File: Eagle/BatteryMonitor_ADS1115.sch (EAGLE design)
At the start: 15 parts, among them IC1 MCP1703CB

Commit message: Optimize part placement
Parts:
- C2, C3, C5: value 100n -> 1µ
- C4: value 100n -> 2µ
- C7: value 100n -> 10µ
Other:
- moved on the sheet: C5
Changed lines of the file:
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@@
 <?xml version="1.0" encoding="utf-8"?>
 <!DOCTYPE eagle SYSTEM "eagle.dtd">
-<eagle version="7.2.0">
+<eagle version="9.6.2">
 <drawing>
 <settings>
 <setting alwaysvectorfont="no"/>
+<setting keepoldvectorfont="yes"/>
 <setting verticaltext="up"/>
 </settings>
@@
 <part name="R2" library="eagle-ltspice" deviceset="R" device="R1206" value="10k"/>
 <part name="C1" library="rcl" deviceset="C-EU" device="C1206" value="100n"/>
-<part name="C2" library="rcl" deviceset="C-EU" device="C1206" value="100n"/>
-<part name="C3" library="rcl" deviceset="C-EU" device="C1206" value="100n"/>
-<part name="C4" library="rcl" deviceset="C-EU" device="C1206" value="100n"/>
+<part name="C2" library="rcl" deviceset="C-EU" device="C1206" value="1µ"/>
+<part name="C3" library="rcl" deviceset="C-EU" device="C1206" value="1µ"/>
+<part name="C4" library="rcl" deviceset="C-EU" device="C1206" value="2µ"/>
 <part name="GND1" library="supply1" deviceset="GND" device=""/>
 <part name="P+1" library="supply1" deviceset="VCC" device=""/>
 <part name="D1" library="diode" deviceset="CGRM400*-G" device="" technology="1"/>
-<part name="C7" library="resistor" deviceset="C-EU" device="C4532" value="100n"/>
+<part name="C7" library="resistor" deviceset="C-EU" device="C4532" value="10µ"/>
 <part name="IC1" library="linear" deviceset="MCP1703" device="CB"/>
-<part name="C5" library="rcl" deviceset="C-EU" device="C1206" value="100n"/>
+<part name="C5" library="rcl" deviceset="C-EU" device="C1206" value="1µ"/>
 </parts>
 <sheets>
@@
 </plain>
 <instances>
-<instance part="U$1" gate="G$1" x="101.6" y="66.04"/>
-<instance part="HSTS016L" gate="A" x="152.4" y="2.54"/>
-<instance part="PWR" gate="-1" x="-7.62" y="43.18">
+<instance part="U$1" gate="G$1" x="101.6" y="66.04" smashed="yes">
+<attribute name="NAME" x="99.06" y="88.9" size="1.27" layer="95"/>
+<attribute name="VALUE" x="99.06" y="86.36" size="1.27" layer="96"/>
+</instance>
+<instance part="HSTS016L" gate="A" x="152.4" y="2.54" smashed="yes">
+<attribute name="NAME" x="146.05" y="10.795" size="1.778" layer="95"/>
+<attribute name="VALUE" x="146.05" y="-5.08" size="1.778" layer="96"/>
+</instance>
+<instance part="PWR" gate="-1" x="-7.62" y="43.18" smashed="yes">
 <attribute name="VIN" x="-7.62" y="38.1" size="1.778" layer="96"/>
-</instance>
-<instance part="PWR" gate="-2" x="-7.62" y="48.26">
+<attribute name="NAME" x="-7.62" y="44.069" size="1.778" layer="95" rot="R180"/>
+</instance>
+<instance part="PWR" gate="-2" x="-7.62" y="48.26" smashed="yes">
 <attribute name="GND" x="-7.62" y="50.8" size="1.778" layer="96" display="name"/>
-</instance>
-<instance part="U$2" gate="G$1" x="101.6" y="7.62"/>
-<instance part="U$3" gate="G$1" x="48.26" y="53.34"/>
-<instance part="R1" gate="G$1" x="17.78" y="30.48" rot="R90"/>
-<instance part="R2" gate="G$1" x="17.78" y="12.7" rot="R90"/>
-<instance part="C1" gate="G$1" x="27.94" y="12.7"/>
-<instance part="C2" gate="G$1" x="30.48" y="83.82"/>
-<instance part="C3" gate="G$1" x="50.8" y="83.82"/>
-<instance part="C4" gate="G$1" x="40.64" y="83.82"/>
-<instance part="GND1" gate="1" x="30.48" y="71.12"/>
-<instance part="P+1" gate="VCC" x="30.48" y="96.52"/>
-<instance part="D1" gate="G$1" x="7.62" y="43.18"/>
-<instance part="C7" gate="G$1" x="17.78" y="81.28" rot="R180"/>
-<instance part="IC1" gate="G$1" x="53.34" y="27.94"/>
-<instance part="C5" gate="G$1" x="7.62" y="83.82"/>
+<attribute name="VALUE" x="-10.16" y="44.577" size="1.778" layer="96"/>
+<attribute name="NAME" x="-7.62" y="49.149" size="1.778" layer="95" rot="R180"/>
+</instance>
+<instance part="U$2" gate="G$1" x="101.6" y="7.62" smashed="yes">
+<attribute name="NAME" x="91.44" y="22.86" size="1.27" layer="94"/>
+<attribute name="VALUE" x="91.44" y="20.32" size="1.27" layer="94"/>
+</instance>
+<instance part="U$3" gate="G$1" x="48.26" y="53.34" smashed="yes">
+<attribute name="NAME" x="33.02" y="55.88" size="1.27" layer="94"/>
+<attribute name="VALUE" x="33.02" y="35.56" size="1.27" layer="94"/>
+</instance>
+<instance part="R1" gate="G$1" x="17.78" y="30.48" smashed="yes" rot="R90">
+<attribute name="NAME" x="16.2814" y="26.67" size="1.778" layer="95" rot="R90"/>
+<attribute name="VALUE" x="21.082" y="26.67" size="1.778" layer="96" rot="R90"/>
+</instance>
+<instance part="R2" gate="G$1" x="17.78" y="12.7" smashed="yes" rot="R90">
+<attribute name="NAME" x="16.2814" y="8.89" size="1.778" layer="95" rot="R90"/>
+<attribute name="VALUE" x="21.082" y="8.89" size="1.778" layer="96" rot="R90"/>
+</instance>
+<instance part="C1" gate="G$1" x="27.94" y="12.7" smashed="yes">
+<attribute name="NAME" x="29.464" y="13.081" size="1.778" layer="95"/>
+<attribute name="VALUE" x="29.464" y="8.001" size="1.778" layer="96"/>
+</instance>
+<instance part="C2" gate="G$1" x="30.48" y="83.82" smashed="yes">
+<attribute name="NAME" x="32.004" y="84.201" size="1.778" layer="95"/>
+<attribute name="VALUE" x="32.004" y="79.121" size="1.778" layer="96"/>
+</instance>
+<instance part="C3" gate="G$1" x="50.8" y="83.82" smashed="yes">
+<attribute name="NAME" x="52.324" y="84.201" size="1.778" layer="95"/>
+<attribute name="VALUE" x="52.324" y="79.121" size="1.778" layer="96"/>
+</instance>
+<instance part="C4" gate="G$1" x="40.64" y="83.82" smashed="yes">
+<attribute name="NAME" x="42.164" y="84.201" size="1.778" layer="95"/>
+<attribute name="VALUE" x="42.164" y="79.121" size="1.778" layer="96"/>
+</instance>
+<instance part="GND1" gate="1" x="30.48" y="71.12" smashed="yes">
+<attribute name="VALUE" x="27.94" y="68.58" size="1.778" layer="96"/>
+</instance>
+<instance part="P+1" gate="VCC" x="30.48" y="96.52" smashed="yes">
+<attribute name="VALUE" x="27.94" y="93.98" size="1.778" layer="96" rot="R90"/>
+</instance>
+<instance part="D1" gate="G$1" x="7.62" y="43.18" smashed="yes">
+<attribute name="NAME" x="10.16" y="43.6626" size="1.778" layer="95"/>
+<attribute name="VALUE" x="10.16" y="40.8686" size="1.778" layer="96"/>
+</instance>
+<instance part="C7" gate="G$1" x="17.78" y="81.28" smashed="yes" rot="R180">
+<attribute name="NAME" x="16.256" y="80.899" size="1.778" layer="95" rot="R180"/>
+<attribute name="VALUE" x="16.256" y="85.979" size="1.778" layer="96" rot="R180"/>
+</instance>
+<instance part="IC1" gate="G$1" x="53.34" y="27.94" smashed="yes">
+<attribute name="NAME" x="45.72" y="33.655" size="1.778" layer="95"/>
+<attribute name="VALUE" x="45.72" y="31.115" size="1.778" layer="96"/>
+</instance>
+<instance part="C5" gate="G$1" x="2.54" y="83.82" smashed="yes">
+<attribute name="NAME" x="4.064" y="84.201" size="1.778" layer="95"/>
+<attribute name="VALUE" x="4.064" y="79.121" size="1.778" layer="96"/>
+</instance>
 </instances>
 <busses>
@@
 <wire x1="50.8" y1="73.66" x2="50.8" y2="78.74" width="0.1524" layer="91"/>
 <pinref part="C5" gate="G$1" pin="2"/>
-<wire x1="7.62" y1="78.74" x2="7.62" y2="73.66" width="0.1524" layer="91"/>
-<wire x1="7.62" y1="73.66" x2="17.78" y2="73.66" width="0.1524" layer="91"/>
+<wire x1="2.54" y1="78.74" x2="2.54" y2="73.66" width="0.1524" layer="91"/>
+<wire x1="2.54" y1="73.66" x2="17.78" y2="73.66" width="0.1524" layer="91"/>
 <junction x="40.64" y="73.66"/>
 <junction x="17.78" y="73.66"/>
@@
 <wire x1="17.78" y1="88.9" x2="17.78" y2="86.36" width="0.1524" layer="91"/>
 <pinref part="C5" gate="G$1" pin="1"/>
-<wire x1="7.62" y1="86.36" x2="7.62" y2="88.9" width="0.1524" layer="91"/>
-<wire x1="7.62" y1="88.9" x2="17.78" y2="88.9" width="0.1524" layer="91"/>
+<wire x1="2.54" y1="86.36" x2="2.54" y2="88.9" width="0.1524" layer="91"/>
+<wire x1="2.54" y1="88.9" x2="17.78" y2="88.9" width="0.1524" layer="91"/>
 <junction x="17.78" y="88.9"/>
 </segment>

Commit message: Change layout - all SMD on top
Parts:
- renumbered HSTS016L to I-SENS, U$1 to ESP32
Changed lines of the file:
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@@
 </classes>
 <parts>
-<part name="U$1" library="MH-ET_ESP32_D1_MINI" deviceset="MH-ET_ESP32_D1_MINI" device=""/>
-<part name="HSTS016L" library="pinhead" deviceset="PINHD-1X4" device="/90" value="1"/>
+<part name="ESP32" library="MH-ET_ESP32_D1_MINI" deviceset="MH-ET_ESP32_D1_MINI" device=""/>
+<part name="I-SENS" library="pinhead" deviceset="PINHD-1X4" device="/90" value="1"/>
 <part name="PWR" library="con-wago-500" deviceset="W237-102" device="" value="12V">
 <attribute name="GND" value=""/>
@@
 </plain>
 <instances>
-<instance part="U$1" gate="G$1" x="101.6" y="66.04" smashed="yes">
+<instance part="ESP32" gate="G$1" x="101.6" y="66.04" smashed="yes">
 <attribute name="NAME" x="99.06" y="88.9" size="1.27" layer="95"/>
 <attribute name="VALUE" x="99.06" y="86.36" size="1.27" layer="96"/>
 </instance>
-<instance part="HSTS016L" gate="A" x="152.4" y="2.54" smashed="yes">
+<instance part="I-SENS" gate="A" x="152.4" y="2.54" smashed="yes">
 <attribute name="NAME" x="146.05" y="10.795" size="1.778" layer="95"/>
 <attribute name="VALUE" x="146.05" y="-5.08" size="1.778" layer="96"/>
@@
 <net name="GND" class="0">
 <segment>
-<pinref part="U$1" gate="G$1" pin="GND@1"/>
+<pinref part="ESP32" gate="G$1" pin="GND@1"/>
 <wire x1="86.36" y1="81.28" x2="66.04" y2="81.28" width="0.1524" layer="91"/>
 <wire x1="66.04" y1="81.28" x2="66.04" y2="50.8" width="0.1524" layer="91"/>
@@
 <wire x1="66.04" y1="48.26" x2="66.04" y2="50.8" width="0.1524" layer="91"/>
 <junction x="66.04" y="50.8"/>
-<pinref part="U$1" gate="G$1" pin="GND@2"/>
+<pinref part="ESP32" gate="G$1" pin="GND@2"/>
 <wire x1="116.84" y1="66.04" x2="127" y2="66.04" width="0.1524" layer="91"/>
 <wire x1="127" y1="66.04" x2="127" y2="96.52" width="0.1524" layer="91"/>
@@
 <wire x1="66.04" y1="96.52" x2="66.04" y2="81.28" width="0.1524" layer="91"/>
 <junction x="66.04" y="81.28"/>
-<pinref part="U$1" gate="G$1" pin="GND@3"/>
+<pinref part="ESP32" gate="G$1" pin="GND@3"/>
 <wire x1="116.84" y1="55.88" x2="127" y2="55.88" width="0.1524" layer="91"/>
 <wire x1="127" y1="55.88" x2="127" y2="66.04" width="0.1524" layer="91"/>
@@
 <junction x="66.04" y="48.26"/>
 <wire x1="127" y1="55.88" x2="127" y2="0" width="0.1524" layer="91"/>
-<pinref part="HSTS016L" gate="A" pin="4"/>
+<pinref part="I-SENS" gate="A" pin="4"/>
 <wire x1="127" y1="0" x2="149.86" y2="0" width="0.1524" layer="91"/>
 <pinref part="R2" gate="G$1" pin="1"/>
@@
 <wire x1="66.04" y1="15.24" x2="66.04" y2="27.94" width="0.1524" layer="91"/>
 <wire x1="124.46" y1="27.94" x2="124.46" y2="7.62" width="0.1524" layer="91"/>
-<pinref part="HSTS016L" gate="A" pin="1"/>
+<pinref part="I-SENS" gate="A" pin="1"/>
 <wire x1="124.46" y1="7.62" x2="149.86" y2="7.62" width="0.1524" layer="91"/>
 <pinref part="IC1" gate="G$1" pin="VO"/>
@@
 <net name="N$7" class="0">
 <segment>
-<pinref part="U$1" gate="G$1" pin="IO21"/>
+<pinref part="ESP32" gate="G$1" pin="IO21"/>
 <wire x1="116.84" y1="73.66" x2="134.62" y2="73.66" width="0.1524" layer="91"/>
 <wire x1="134.62" y1="73.66" x2="134.62" y2="22.86" width="0.1524" layer="91"/>
@@
 <net name="N$8" class="0">
 <segment>
-<pinref part="U$1" gate="G$1" pin="IO22"/>
+<pinref part="ESP32" gate="G$1" pin="IO22"/>
 <wire x1="116.84" y1="76.2" x2="129.54" y2="76.2" width="0.1524" layer="91"/>
 <wire x1="129.54" y1="76.2" x2="129.54" y2="25.4" width="0.1524" layer="91"/>
@@
 <segment>
 <pinref part="U$2" gate="G$1" pin="A0"/>
-<pinref part="HSTS016L" gate="A" pin="2"/>
+<pinref part="I-SENS" gate="A" pin="2"/>
 <wire x1="114.3" y1="5.08" x2="149.86" y2="5.08" width="0.1524" layer="91"/>
 </segment>
@@
 <net name="N$6" class="0">
 <segment>
-<pinref part="HSTS016L" gate="A" pin="3"/>
+<pinref part="I-SENS" gate="A" pin="3"/>
 <wire x1="114.3" y1="2.54" x2="149.86" y2="2.54" width="0.1524" layer="91"/>
 <pinref part="U$2" gate="G$1" pin="A1"/>
@@
 <wire x1="68.58" y1="40.64" x2="68.58" y2="91.44" width="0.1524" layer="91"/>
 <wire x1="68.58" y1="91.44" x2="124.46" y2="91.44" width="0.1524" layer="91"/>
-<pinref part="U$1" gate="G$1" pin="VCC"/>
+<pinref part="ESP32" gate="G$1" pin="VCC"/>
 <wire x1="116.84" y1="63.5" x2="124.46" y2="63.5" width="0.1524" layer="91"/>
 <wire x1="124.46" y1="91.44" x2="124.46" y2="63.5" width="0.1524" layer="91"/>

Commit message: Correct description of DCDC output voltage
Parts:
- renumbered PWR to BATTERY
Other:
- note added: "-The DC-DC converter should provide 5.5V - The ESP is powered with 5.5V - The increased voltage is needed in order for the MCP1703 to provide stable 5V to the ADS1115 and the current sensor"
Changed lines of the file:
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@@
 <part name="ESP32" library="MH-ET_ESP32_D1_MINI" deviceset="MH-ET_ESP32_D1_MINI" device=""/>
 <part name="I-SENS" library="pinhead" deviceset="PINHD-1X4" device="/90" value="1"/>
-<part name="PWR" library="con-wago-500" deviceset="W237-102" device="" value="12V">
+<part name="BATTERY" library="con-wago-500" deviceset="W237-102" device="" value="12V">
 <attribute name="GND" value=""/>
 <attribute name="VIN" value="12V"/>
@@
 <sheet>
 <plain>
+<text x="142.24" y="63.5" size="2.1844" layer="97">-The DC-DC converter should provide 5.5V
+- The ESP is powered with 5.5V
+- The increased voltage is needed in order for the
+MCP1703 to provide stable 5V to the ADS1115
+and the current sensor</text>
 </plain>
 <instances>
@@
 <attribute name="VALUE" x="146.05" y="-5.08" size="1.778" layer="96"/>
 </instance>
-<instance part="PWR" gate="-1" x="-7.62" y="43.18" smashed="yes">
+<instance part="BATTERY" gate="-1" x="-7.62" y="43.18" smashed="yes">
 <attribute name="VIN" x="-7.62" y="38.1" size="1.778" layer="96"/>
 <attribute name="NAME" x="-7.62" y="44.069" size="1.778" layer="95" rot="R180"/>
 </instance>
-<instance part="PWR" gate="-2" x="-7.62" y="48.26" smashed="yes">
+<instance part="BATTERY" gate="-2" x="-7.62" y="48.26" smashed="yes">
 <attribute name="GND" x="-7.62" y="50.8" size="1.778" layer="96" display="name"/>
 <attribute name="VALUE" x="-10.16" y="44.577" size="1.778" layer="96"/>
@@
 <pinref part="U$3" gate="G$1" pin="IN-@2"/>
 <wire x1="25.4" y1="48.26" x2="22.86" y2="48.26" width="0.1524" layer="91"/>
-<pinref part="PWR" gate="-2" pin="KL"/>
+<pinref part="BATTERY" gate="-2" pin="KL"/>
 <junction x="22.86" y="48.26"/>
 <wire x1="-2.54" y1="48.26" x2="22.86" y2="48.26" width="0.1524" layer="91"/>
@@
 <net name="N$1" class="0">
 <segment>
-<pinref part="PWR" gate="-1" pin="KL"/>
+<pinref part="BATTERY" gate="-1" pin="KL"/>
 <pinref part="D1" gate="G$1" pin="A"/>
 <wire x1="2.54" y1="43.18" x2="5.08" y2="43.18" width="0.1524" layer="91"/>
@@
 </schematic>
 </drawing>
+<compatibility>
+<note version="6.3" minversion="6.2.2" severity="warning">
+Since Version 6.2.2 text objects can contain more than one line,
+which will not be processed correctly with this version.
+</note>
+</compatibility>
 </eagle>

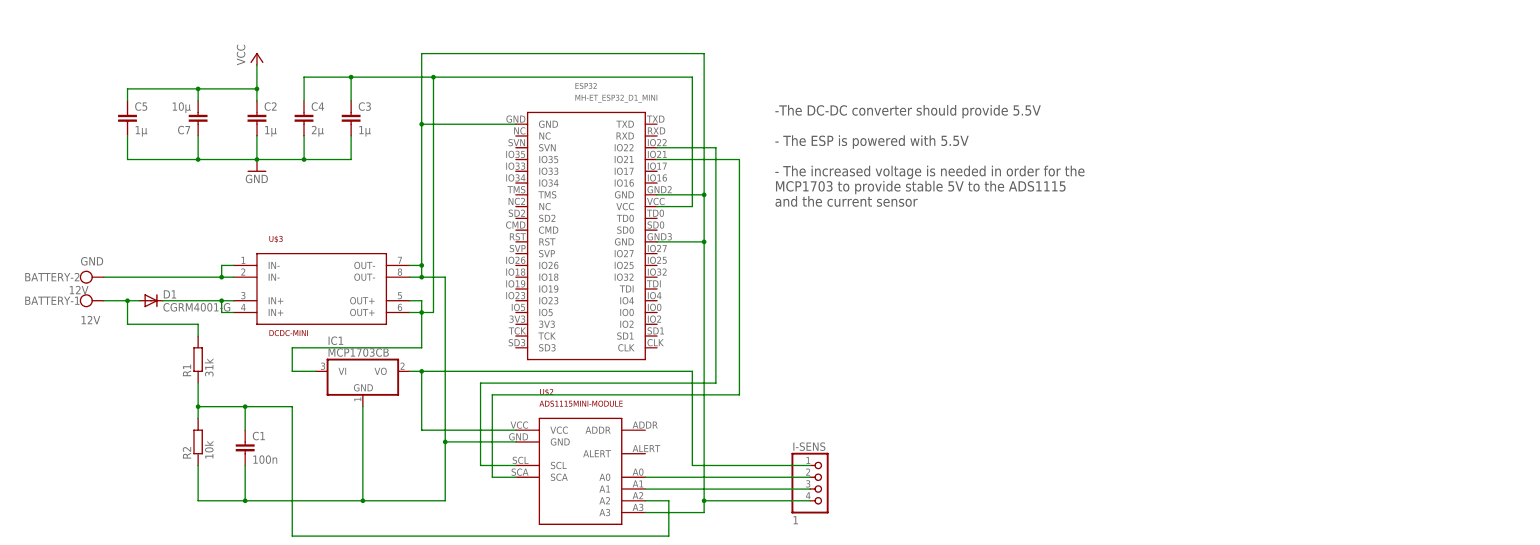
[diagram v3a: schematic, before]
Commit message: Update layout: add 3.3V to IO connector
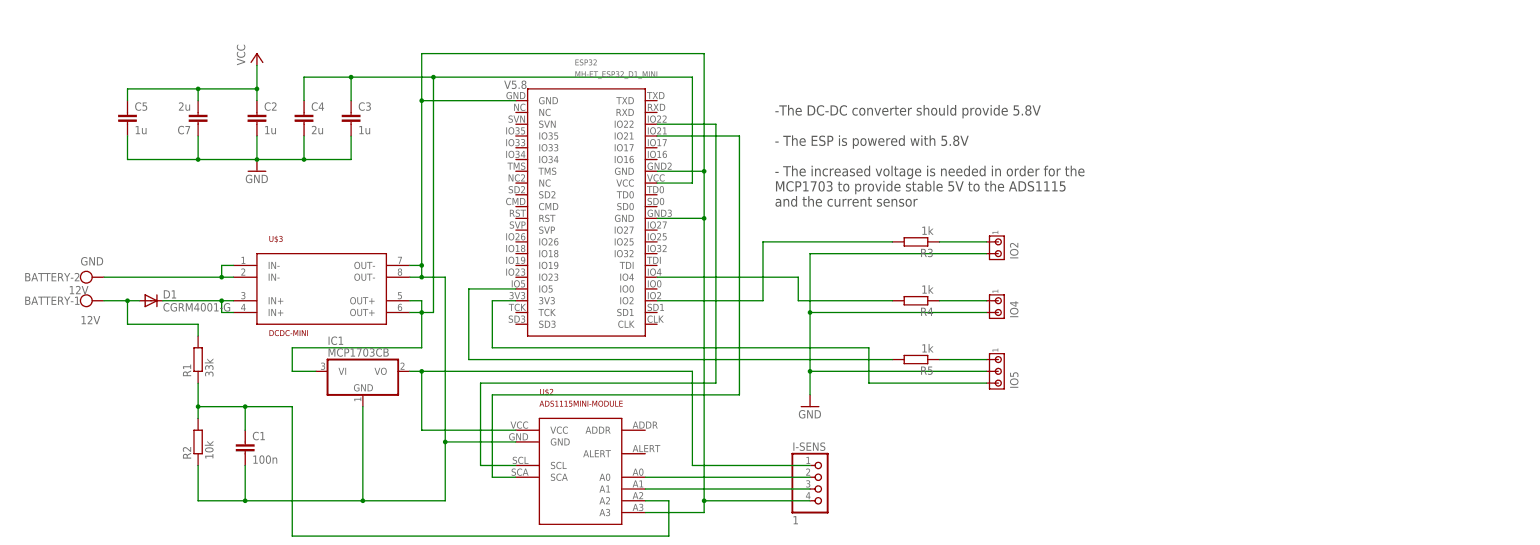
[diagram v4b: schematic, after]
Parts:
- added IO2, IO4: (no value), con-amp:MTA02-100
- added IO5: (no value), con-amp:MTA03-100
- added R3, R4, R5: 1k, eagle-ltspice:RR1206
- C2, C3, C5: value 1µ -> 1u
- C4: value 2µ -> 2u
- C7: value 10µ -> 2u; device resistor:C-EUC4532 -> rcl:C-EUC1206
- R1: value 31k -> 33k
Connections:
- net N$1 renamed 12V
- net V5.5 renamed V5.8
- new net N$1: IO5.1, R5.1
- new net N$10: IO4.1, R4.1
- new net N$11: IO2.1, R3.1
- new net N$12: ESP32.3V3, IO5.3
- new net N$2: ESP32.IO2, R3.2
- new net N$3: ESP32.IO4, R4.2
- new net N$5: ESP32.IO5, R5.2
- net GND: now also IO2.2, IO4.2, IO5.2
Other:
- note added: "-The DC-DC converter should provide 5.8V - The ESP is powered with 5.8V - The increased voltage is needed in order for the MCP1703 to provide stable 5V to the ADS1115 and the current sensor"
- note removed: "-The DC-DC converter should provide 5.5V - The ESP is powered with 5.5V - The increased voltage is needed in order for the MCP1703 to provide stable 5V to the ADS1115 and the current sensor"
- moved on the sheet: ESP32

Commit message: Calibration done and documented
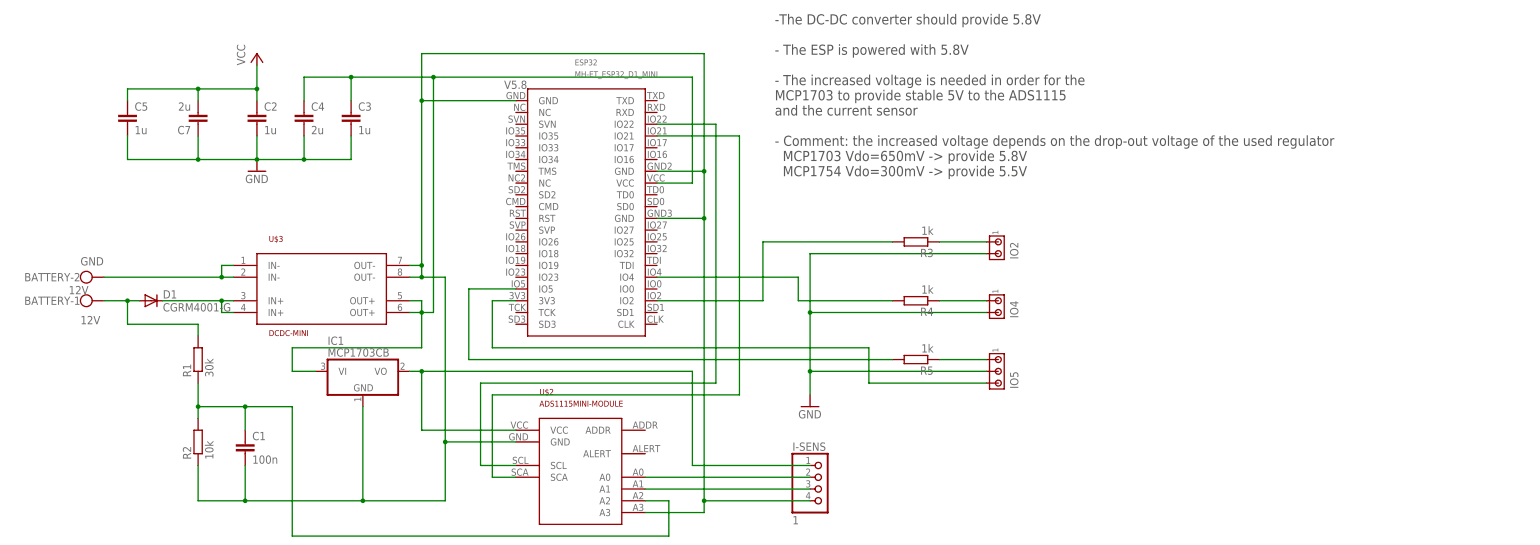
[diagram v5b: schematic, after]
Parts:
- R1: value 33k -> 30k
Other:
- note added: "-The DC-DC converter should provide 5.8V - The ESP is powered with 5.8V - The increased voltage is needed in order for the MCP1703 to provide stable 5V to the ADS1115 and the current sensor - Comment: the increased voltage depends on the drop-out voltage of the used regulator MCP1703 Vdo=650mV -> provide 5.8V MCP1754 Vdo=300mV -> provide 5.5V"
- note removed: "-The DC-DC converter should provide 5.8V - The ESP is powered with 5.8V - The increased voltage is needed in order for the MCP1703 to provide stable 5V to the ADS1115 and the current sensor"
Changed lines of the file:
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@@
 <part name="U$2" library="monitor_components" deviceset="ADS1115" device="MINI-MODULE"/>
 <part name="U$3" library="monitor_components" deviceset="DCDC-MINI" device=""/>
-<part name="R1" library="eagle-ltspice" deviceset="R" device="R1206" value="33k"/>
+<part name="R1" library="eagle-ltspice" deviceset="R" device="R1206" value="30k"/>
 <part name="R2" library="eagle-ltspice" deviceset="R" device="R1206" value="10k"/>
 <part name="C1" library="rcl" deviceset="C-EU" device="C1206" value="100n"/>
@@
 - The increased voltage is needed in order for the
 MCP1703 to provide stable 5V to the ADS1115
-and the current sensor</text>
+and the current sensor
+- Comment: the increased voltage depends on the drop-out voltage of the used regulator
+  MCP1703 Vdo=650mV -&gt; provide 5.8V
+  MCP1754 Vdo=300mV -&gt; provide 5.5V
+  </text>
 </plain>
 <instances>
